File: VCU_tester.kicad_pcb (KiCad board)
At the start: 2 copper layers, 54.6 x 21.6 mm, 93 parts, among them J1 Conn_01x04_Male, J10 DB9_Male, J11 DB9_Male, J12 Conn_01x08_Male, J13 Conn_01x08_Male, J2 Screw_Terminal_01x02, J3 DB9_Male, J4 DB9_Male, J5 DB9_Male, J500 Conn_01x08_Female, J501 Conn_01x08_Female, J502 Conn_01x08_Female, J504 Conn_02x18_Odd_Even, J505 Conn_01x10_Female, J506 Conn_01x08_Female, J507 Conn_01x08_Female, J6 DB9_Male, J7 Conn_01x04_Male, J8 DB9_Male, J9 DB9_Male, P8 BeagleBone_Black_Header, P9 BeagleBone_Black_Header, U1 REF3020, U2 MAX3232, U3 TCAN1042HVD, U4 MAX3232, U5 TCAN1042HVD

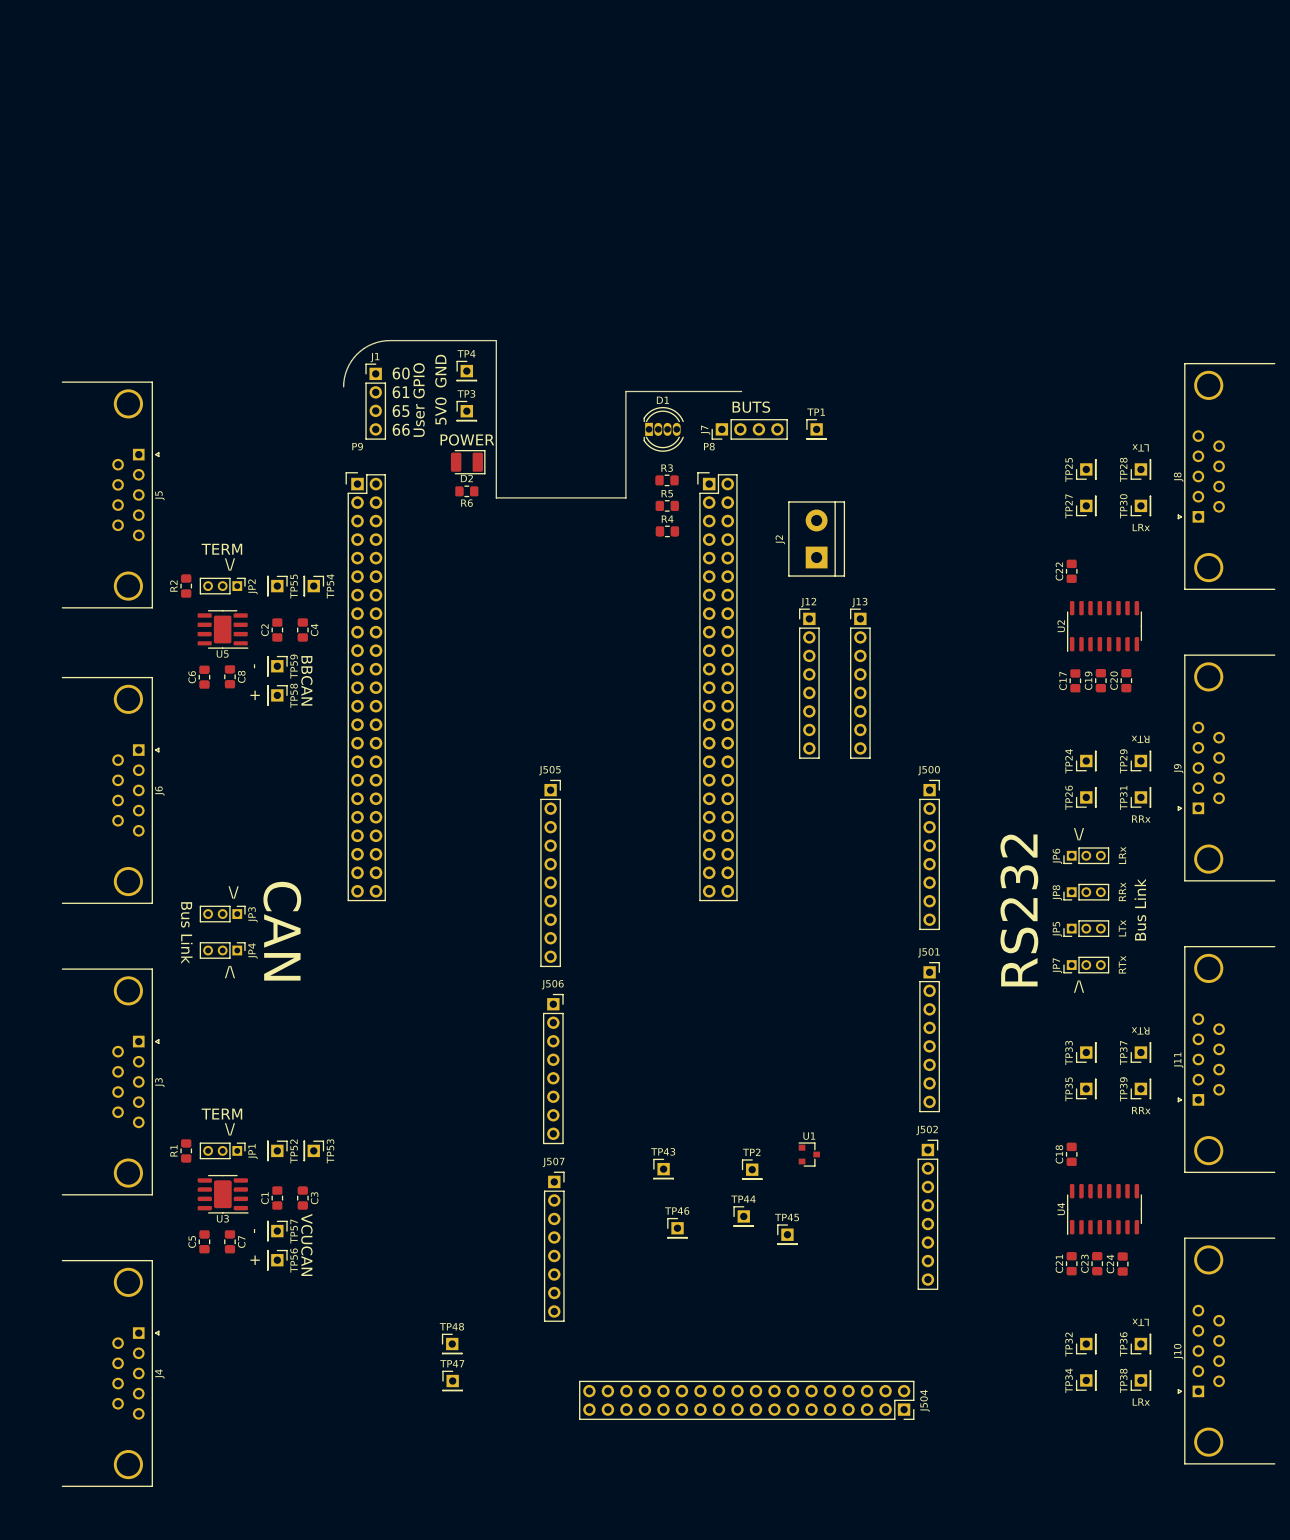
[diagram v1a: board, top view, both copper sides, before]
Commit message: added worksheet, shuffled board around to make it smaller
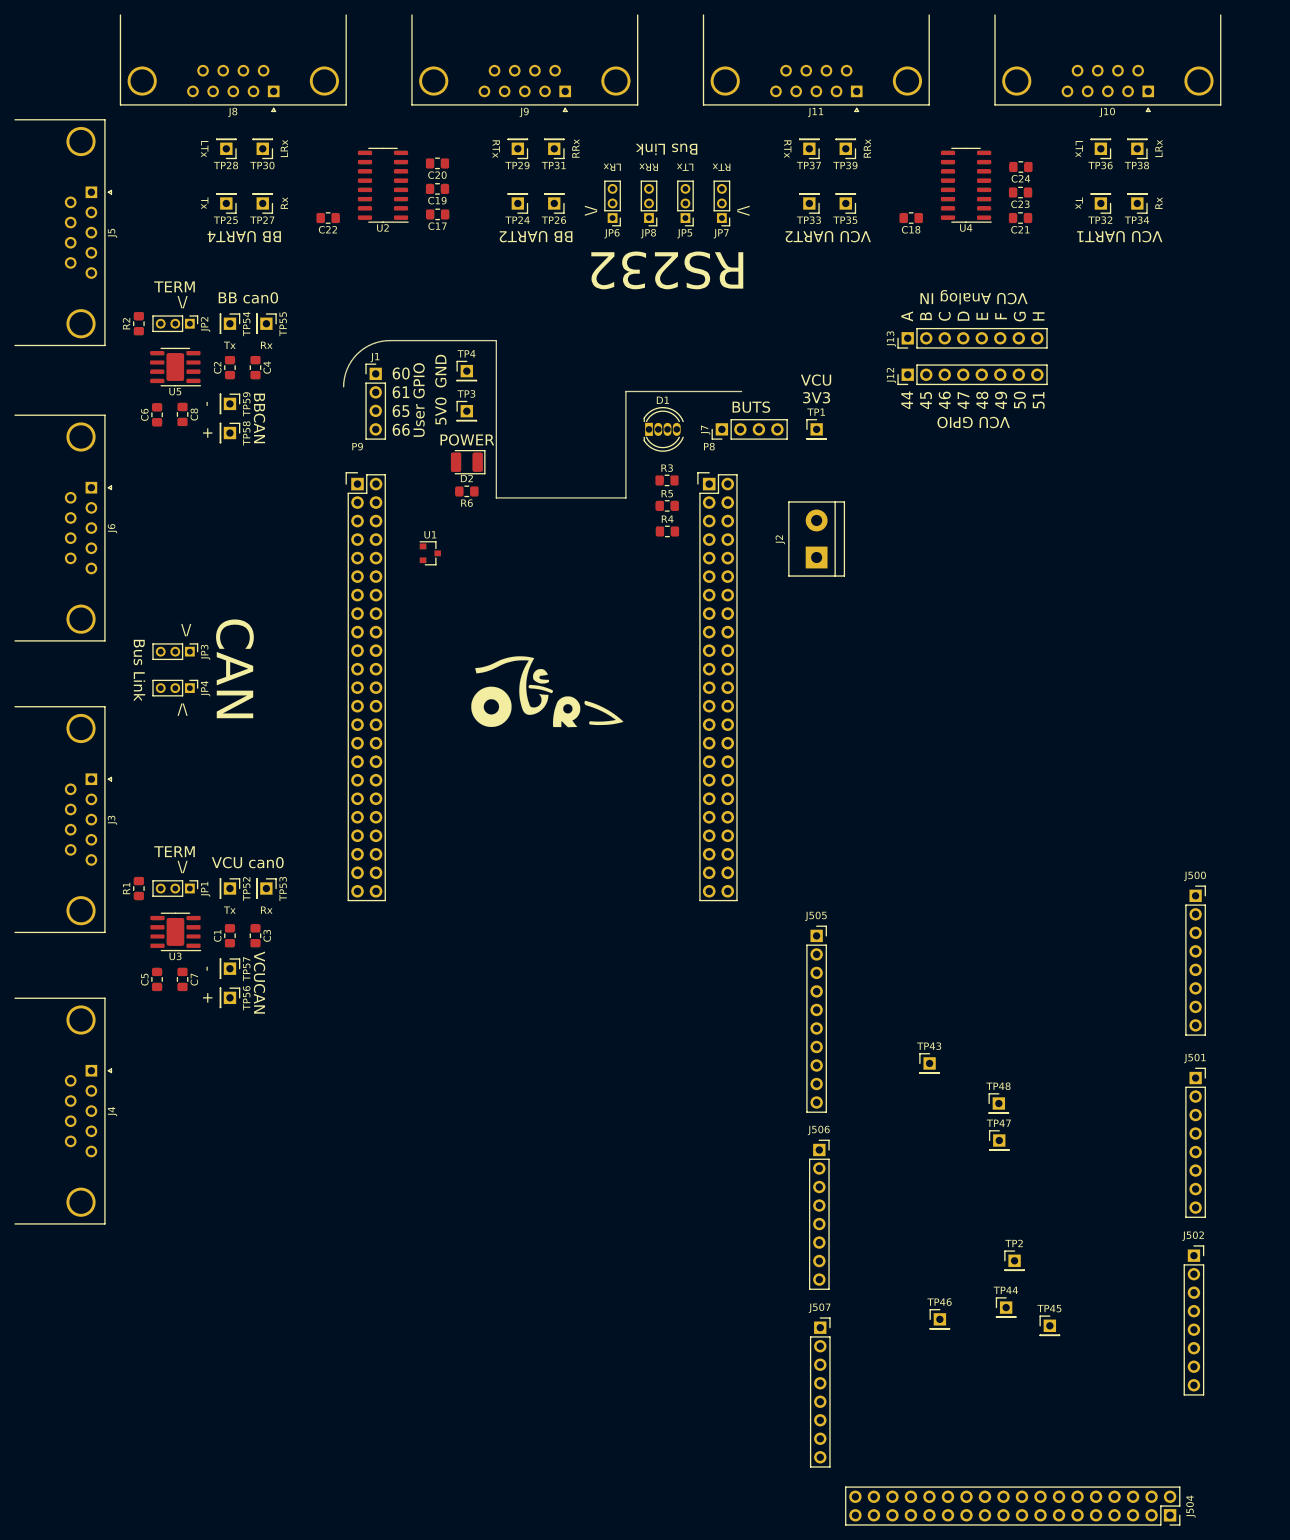
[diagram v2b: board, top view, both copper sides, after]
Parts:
- added G***: LOGO, footprints:OUR-Logo, F.Cu at (113.9, 68.9)
- moved J10 178.5 mm to (196.4, -13.5), turned to 180 degrees
- moved TP38 169.0 mm to (194.9, -5.62), turned to 180 degrees
- moved TP36 164.1 mm to (189.9, -5.62), turned to 180 degrees
- moved TP34 161.7 mm to (194.9, 1.88), turned to 180 degrees
- moved TP32 156.5 mm to (189.9, 1.88), turned to 180 degrees
- moved C24 151.2 mm to (178.9, -3.12), turned to 180 degrees
- moved C23 147.4 mm to (178.8, 0.38), turned to 180 degrees
- moved J11 146.1 mm to (156.4, -13.5), turned to 180 degrees
- moved C21 143.6 mm to (178.8, 3.88), turned to 180 degrees
- moved U4 141.8 mm to (171.4, -0.62), turned to 180 degrees
- moved J8 139.7 mm to (76.4, -13.5), turned to 180 degrees
- moved TP39 135.2 mm to (154.9, -5.62), turned to 180 degrees
- moved TP28 133.0 mm to (69.9, -5.62), turned to 180 degrees
- moved TP37 132.1 mm to (149.9, -5.62), turned to 180 degrees
- moved J9 131.2 mm to (116.4, -13.5), turned to 180 degrees
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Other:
- board text added: "44 45 46 47 48 49 50 51"
- board text added: "A B C D E F G H"
- board text added: "BB UART2"
- board text added: "BB UART4"
- board text added: "BB can0"
- board text added: "Rx"
- board text added: "Tx"
- board text added: "VCU 3V3"
- board text added: "VCU Analog IN"
- board text added: "VCU GPIO"
- board text added: "VCU UART1"
- board text added: "VCU UART2"
- board text added: "VCU can0"
- board text removed: "Beagle side"
- board text removed: "VCU side"

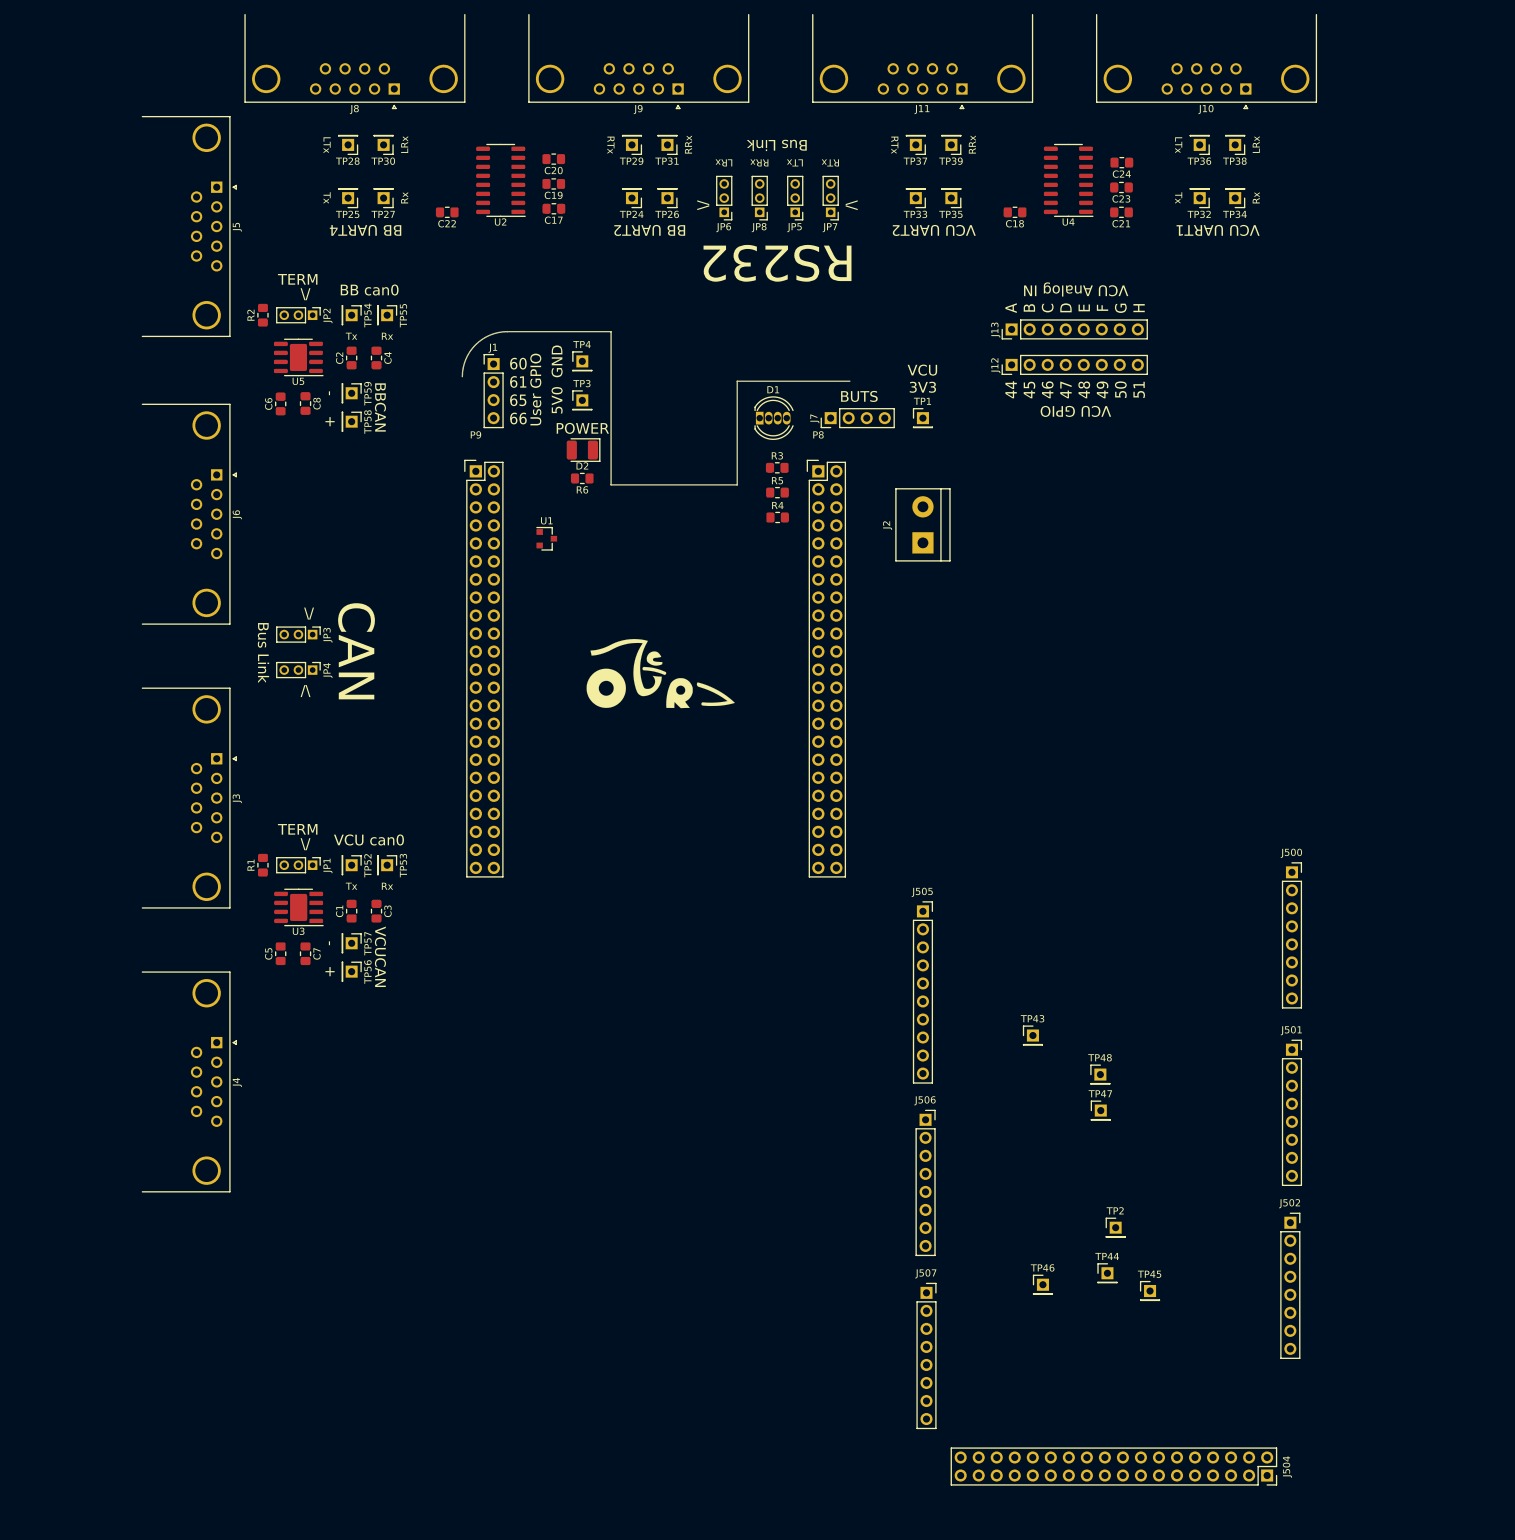
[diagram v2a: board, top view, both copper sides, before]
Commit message: pins corrected, RTC added
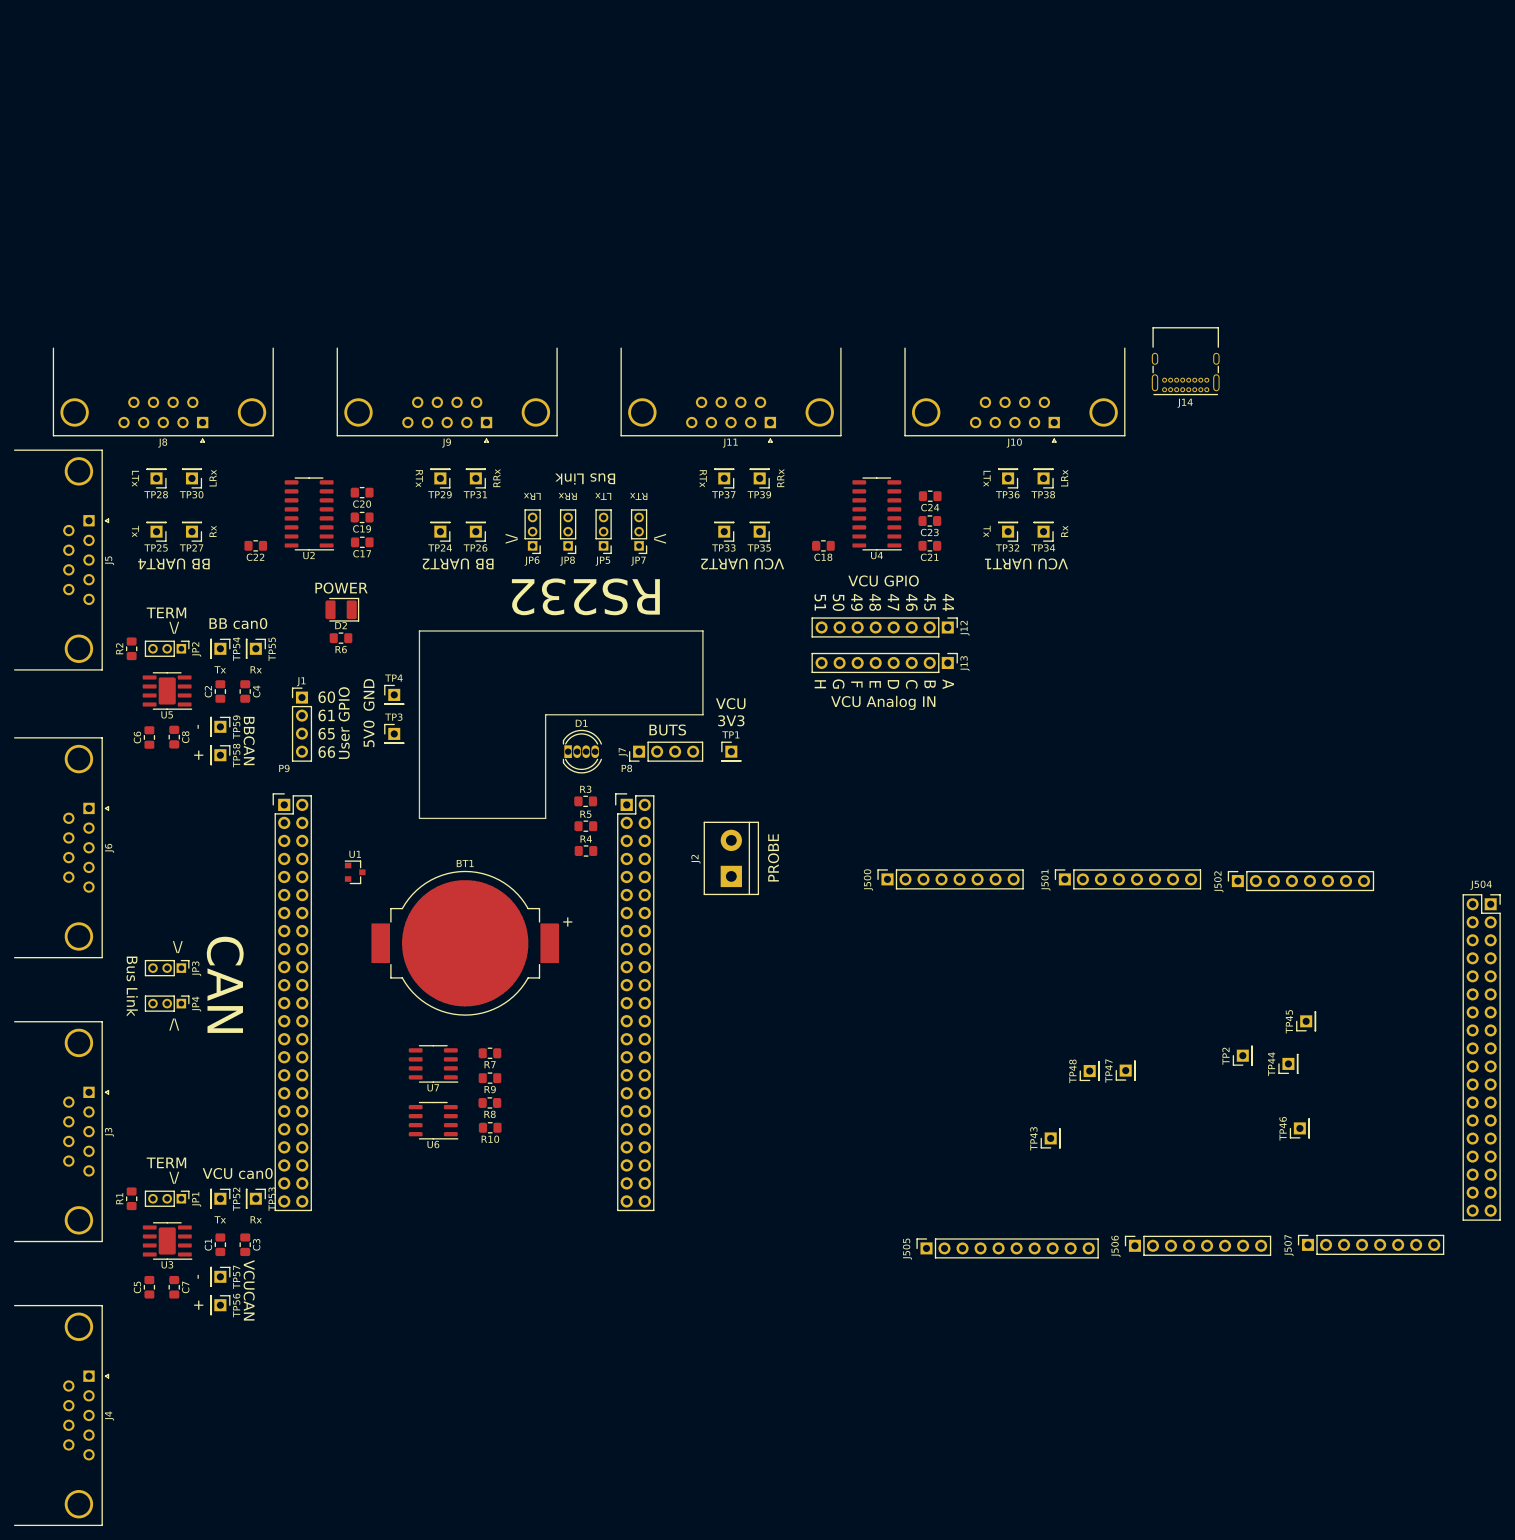
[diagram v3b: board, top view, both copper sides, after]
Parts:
- removed G***: LOGO, footprints:OUR-Logo
- added BT1: Battery_Cell, Battery:BatteryHolder_MPD_BC2003_1x2032, F.Cu at (86.4, 106.9)
- added J14: USB_C_Receptacle, Connector_USB:USB_C_Receptacle_GCT_USB4085, F.Cu at (190.9, 28.9)
- added R10: 4K7, Resistor_SMD:R_0805_2012Metric_Pad1.15x1.40mm_HandSolder, F.Cu at (89.9, 132.9)
- added R7: 4K7, Resistor_SMD:R_0805_2012Metric_Pad1.15x1.40mm_HandSolder, F.Cu at (89.9, 122.4)
- added R8: 4K7, Resistor_SMD:R_0805_2012Metric_Pad1.15x1.40mm_HandSolder, F.Cu at (89.8, 129.4)
- added R9: 4K7, Resistor_SMD:R_0805_2012Metric_Pad1.15x1.40mm_HandSolder, F.Cu at (89.9, 125.9)
- added U6: DS3231MZ, Package_SO:SOIC-8_3.9x4.9mm_P1.27mm, F.Cu at (81.9, 131.9)
- added U7: DS3231MZ, Package_SO:SOIC-8_3.9x4.9mm_P1.27mm, F.Cu at (81.9, 123.9)
- moved J504 86.4 mm to (230.9, 101.4), turned to 0 degrees
- moved J500 57.0 mm to (145.9, 97.9), turned to 90 degrees
- moved D1 54.2 mm to (100.9, 79.9)
- moved J7 54.2 mm to (110.9, 79.9)
- moved P8 54.2 mm to (109.1, 87.4)
- moved R3 54.2 mm to (103.3, 86.9)
- moved R4 54.2 mm to (103.4, 93.9)
- moved R5 54.2 mm to (103.4, 90.4)
- moved TP1 54.2 mm to (123.9, 79.9)
- moved U1 54.2 mm to (70.9, 96.9)
- moved C17 54.2 mm to (71.9, 50.4)
- moved C18 54.2 mm to (136.8, 50.9)
- moved C19 54.2 mm to (71.8, 46.9)
- moved C20 54.2 mm to (71.8, 43.4)
- moved C21 54.2 mm to (151.8, 50.9)
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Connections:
- J507 pad 1: Net-(J507-Pad1) -> /PD28
- J507 pad 2: Net-(J507-Pad2) -> /PD27
- P9 pad 17: /DCAN0_RX -> /GPIO_5
- P9 pad 18: /DCAN0_TX -> /GPIO_4
- P9 pad 19: /UART1_RTSN -> /DCAN0_RX
- P9 pad 20: /UART1_CTSN -> /DCAN0_TX
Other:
- board size 54.6 x 21.6 mm -> 39.9 x 26.4 mm
- board text added: "PROBE"

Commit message: routing start
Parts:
- moved R7 11.1 mm to (89.8, 133.5)
- moved R10 6.00 mm to (89.8, 126.9)
- moved R8 6.00 mm to (89.8, 123.4)
- moved R9 4.37 mm to (89.7, 130.2)
- moved C1 2.55 mm to (49.4, 148.9)
- moved C2 2.55 mm to (49.4, 70.9)
- moved C3 2.55 mm to (52.9, 148.9)
- moved C4 2.55 mm to (52.9, 70.9)
- moved C5 2.55 mm to (39.4, 154.9)
- moved C6 2.55 mm to (39.4, 77.4)
- moved C7 2.55 mm to (42.9, 154.9)
- moved C8 2.55 mm to (42.9, 77.3)
- moved J3 2.55 mm to (30.9, 127.4)
- moved J4 2.55 mm to (30.9, 167.4)
- moved J5 2.55 mm to (30.9, 46.8)
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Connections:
- BT1 pad 1: (no net) -> GNDD
- BT1 pad 2: (no net) -> /RTC_VBAT
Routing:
- net GNDD: track 0.00 -> 469.6 mm
- net +5V: track 0.00 -> 219.8 mm, vias 0 -> 1
- net BBCAN-: track 0.00 -> 132.8 mm, vias 0 -> 3
- net BBCAN+: track 0.00 -> 125.9 mm, vias 0 -> 1
- net VCUCAN+: track 0.00 -> 125.9 mm, vias 0 -> 3
- net VCUCAN-: track 0.00 -> 120.8 mm, vias 0 -> 2
- net +3V3: track 0.00 -> 112.2 mm, vias 0 -> 4
- net /motor_controller/VLRX: track 0.00 -> 90.5 mm, vias 0 -> 1
- net +3.3VA: track 0.00 -> 84.6 mm, vias 0 -> 1
- net /motor_controller/BBLTX: track 0.00 -> 81.4 mm, vias 0 -> 2
- net /motor_controller/VLTX: track 0.00 -> 71.9 mm, vias 0 -> 1
- net /motor_controller/BBLRX: track 0.00 -> 63.1 mm, vias 0 -> 1
- net /motor_controller/VRRX: track 0.00 -> 60.9 mm, vias 0 -> 2
- net /motor_controller/BBRTX: track 0.00 -> 57.8 mm
- net /motor_controller/VRTX: track 0.00 -> 49.3 mm
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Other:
- board size 39.9 x 26.4 mm -> 240.2 x 171.8 mm
